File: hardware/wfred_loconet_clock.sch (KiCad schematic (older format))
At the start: 8 parts, among them U101 L6920D

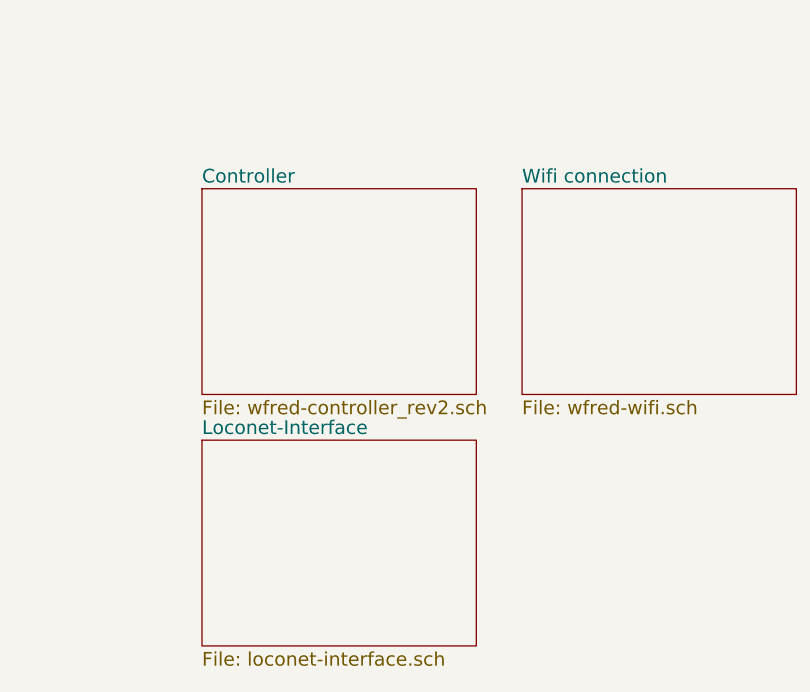
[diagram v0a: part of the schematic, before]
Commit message: Removed wiFred info from from clock project
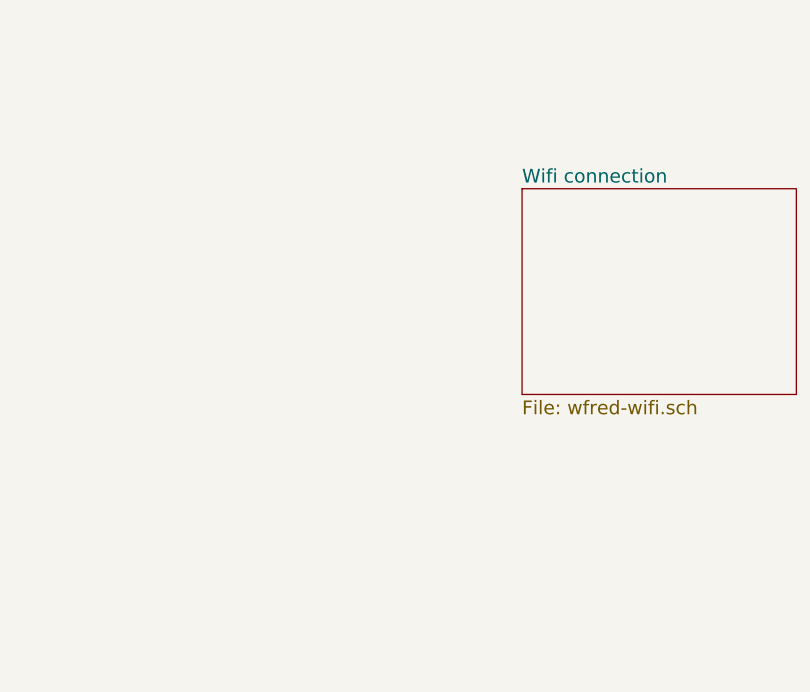
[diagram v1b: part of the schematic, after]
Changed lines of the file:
@@
 $Descr A4 11693 8268
 encoding utf-8
-Sheet 1 5
+Sheet 1 3
 Title "Wireless FREDI (and clock interface)"
 Date "2017-11-19"
@@
 	1    0    0    -1
 $EndComp
-$Sheet
-S 4700 4200 1200 900
-U 5920C945
-F0 "Controller" 60
-F1 "wfred-controller_rev2.sch" 60
-$EndSheet
-$Sheet
-S 4700 5300 1200 900
-U 5920DD06
-F0 "Loconet-Interface" 60
-F1 "loconet-interface.sch" 60
-$EndSheet
 $Comp
 L C C102

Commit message: Fix schematic after untangling from wiFred
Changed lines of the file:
@@
 $EndDescr
-Wire Wire Line
-	2450 2450 2450 2700
-Wire Wire Line
-	900  2600 2450 2600
 Wire Wire Line
 	2150 2400 2150 2700
@@
 Wire Wire Line
 	1500 2800 1850 2800
-Wire Wire Line
-	1850 2450 1850 3300
 Wire Wire Line
 	2150 3100 2150 3300
@@
 	1    0    0    -1
 $EndComp
-$Comp
-L PWR_FLAG #FLG011
-U 1 1 59214833
-P 2450 2450
-F 0 "#FLG011" H 2450 2545 30  0001 C CNN
-F 1 "PWR_FLAG" H 2450 2630 30  0000 C CNN
-F 2 "" H 2450 2450 60  0001 C CNN
-F 3 "" H 2450 2450 60  0001 C CNN
-	1    2450 2450
-	1    0    0    -1
-$EndComp
-Connection ~ 2450 2600
-$Comp
-L PWR_FLAG #FLG012
-U 1 1 59214BB2
-P 1850 2450
-F 0 "#FLG012" H 1850 2545 30  0001 C CNN
-F 1 "PWR_FLAG" H 1850 2630 30  0000 C CNN
-F 2 "" H 1850 2450 60  0001 C CNN
-F 3 "" H 1850 2450 60  0001 C CNN
-	1    1850 2450
-	1    0    0    -1
-$EndComp
-Connection ~ 1850 2800
 $Comp
 L L6920D U101
@@
 	0    1    1    0
 $EndComp
+Wire Wire Line
+	2450 2700 2450 2600
+Wire Wire Line
+	2450 2600 900  2600
+Wire Wire Line
+	1850 2800 1850 3300
 $EndSCHEMATC

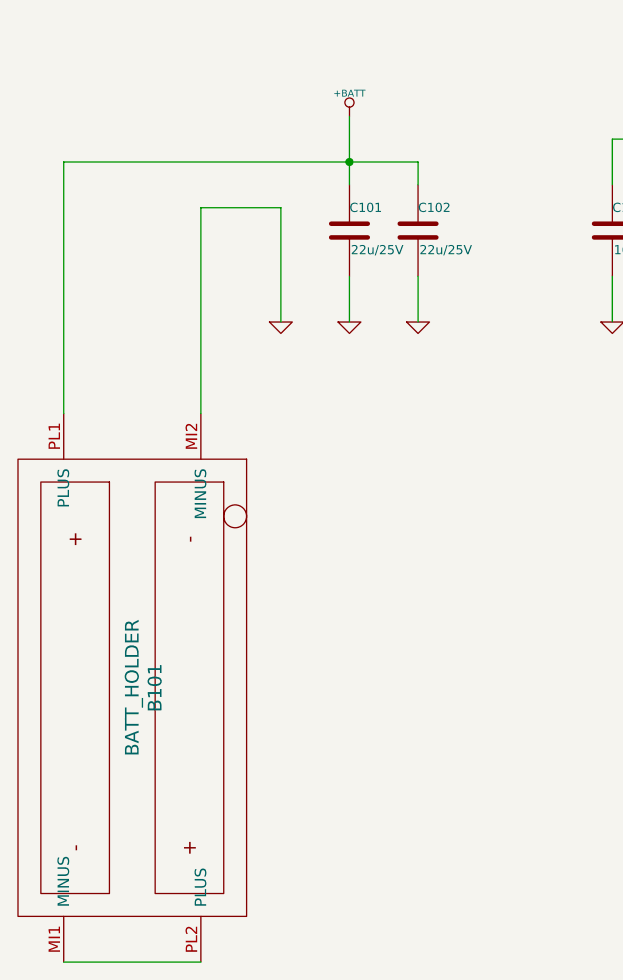
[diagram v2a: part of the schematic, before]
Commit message: Change clock schematic and PCB
- Remove slide switches, replace with single push button
- Add status LED
- Re-add battery measurement connection

- Change PCB form factor to fit NewAgeEnclosures Compact AA housing
- Re-layout PCB
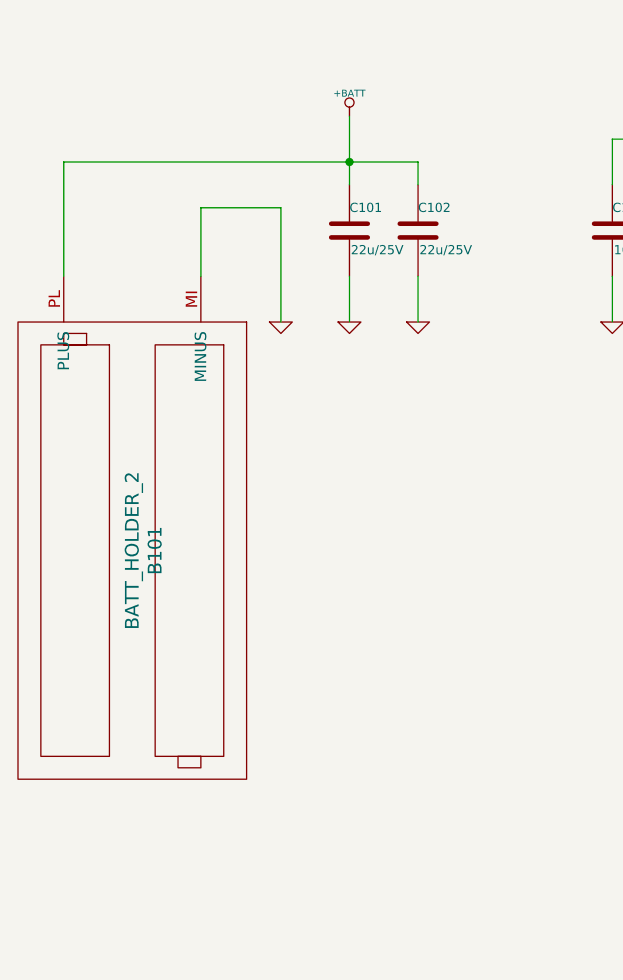
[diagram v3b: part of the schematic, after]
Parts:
- removed B101: BATT_HOLDER, myFootprints:KEYSTONE1013, symbol BATT_HOLDER
- added B101: BATT_HOLDER_2, myFootprints:NEW_AGE_COMPACT_AA_PCBEdges, symbol BATT_HOLDER_2
- L101: footprint myFootprints:L_2424_HandSoldering -> Inductors_SMD:L_Fastron_PISN_Handsoldering
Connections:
- net +BATT: now also B101.PL (PLUS)
- net GND: now also B101.MI (MINUS)
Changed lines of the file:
@@
 Connection ~ 2150 2600
-Wire Wire Line
-	1500 2800 1850 2800
 Wire Wire Line
 	2150 3100 2150 3300
@@
 F 0 "L101" V 4250 1400 40  0000 C CNN
 F 1 "22u" V 4400 1400 40  0000 C CNN
-F 2 "myFootprints:L_2424_HandSoldering" H 4300 1400 60  0001 C CNN
+F 2 "Inductors_SMD:L_Fastron_PISN_Handsoldering" H 4300 1400 60  0001 C CNN
 F 3 "" H 4300 1400 60  0000 C CNN
 F 4 "L-242418FPS 22µ" V 4300 1400 60  0001 C CNN "Reichelt"
@@
 $EndSheet
 Wire Wire Line
-	900  6100 1500 6100
-Wire Wire Line
-	900  3700 900  2600
-Wire Wire Line
-	1500 3700 1500 2800
-$Comp
-L BATT_HOLDER B101
-U 1 1 5A14A6C1
-P 1200 4900
-F 0 "B101" H 1200 5000 60  0000 C CNN
-F 1 "BATT_HOLDER" H 1200 4900 60  0000 C CNN
-F 2 "myFootprints:KEYSTONE1013" H 1200 4900 60  0001 C CNN
-F 3 "" H 1200 4900 60  0001 C CNN
-F 4 "KEYSTONE 1013" H 1200 4900 60  0001 C CNN "Reichelt"
-	1    1200 4900
+	2450 2600 2450 2700
+Wire Wire Line
+	1850 2800 1850 3300
+$Comp
+L BATT_HOLDER_2 B101
+U 1 1 5C82AFB3
+P 1200 4300
+F 0 "B101" H 1200 4400 60  0000 C CNN
+F 1 "BATT_HOLDER_2" H 1200 4300 60  0000 C CNN
+F 2 "myFootprints:NEW_AGE_COMPACT_AA_PCBEdges" H 1200 4300 60  0001 C CNN
+F 3 "" H 1200 4300 60  0001 C CNN
+	1    1200 4300
 	0    1    1    0
 $EndComp
 Wire Wire Line
-	2450 2700 2450 2600
-Wire Wire Line
-	2450 2600 900  2600
-Wire Wire Line
-	1850 2800 1850 3300
+	1500 3100 1500 2800
+Wire Wire Line
+	1500 2800 1850 2800
+Wire Wire Line
+	900  2600 2450 2600
+Wire Wire Line
+	900  2600 900  3100
 $EndSCHEMATC

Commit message: Opened schematic and pcb with kicad 5.1.5...
...to update library table
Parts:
- B101: symbol BATT_HOLDER_2 -> wfred_loconet_clock-rescue:BATT_HOLDER_2
- C101, C102, C103, C104, C105: symbol C -> wfred_loconet_clock-rescue:C
- L101: symbol INDUCTOR -> wfred_loconet_clock-rescue:INDUCTOR
- U101: symbol L6920D -> wfred_loconet_clock-rescue:L6920D
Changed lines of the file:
@@
-EESchema Schematic File Version 2
-LIBS:wfred_loconet_clock-rescue
-LIBS:power
-LIBS:device
-LIBS:transistors
-LIBS:conn
-LIBS:linear
-LIBS:regul
-LIBS:74xx
-LIBS:cmos4000
-LIBS:adc-dac
-LIBS:memory
-LIBS:xilinx
-LIBS:microcontrollers
-LIBS:dsp
-LIBS:microchip
-LIBS:analog_switches
-LIBS:motorola
-LIBS:texas
-LIBS:intel
-LIBS:audio
-LIBS:interface
-LIBS:digital-audio
-LIBS:philips
-LIBS:display
-LIBS:cypress
-LIBS:siliconi
-LIBS:opto
-LIBS:atmel
-LIBS:contrib
-LIBS:valves
-LIBS:my_devices
-LIBS:ESP8266
-LIBS:wfred_loconet_clock-cache
-EELAYER 25 0
+EESchema Schematic File Version 4
+EELAYER 30 0
 EELAYER END
 $Descr A4 11693 8268
@@
 $EndDescr
 Wire Wire Line
-	2150 2400 2150 2700
+	2150 2400 2150 2600
 Connection ~ 2150 2600
 Wire Wire Line
@@
 	3300 3100 3300 3300
 Wire Wire Line
-	5200 2000 5200 2800
-Wire Wire Line
-	5000 2200 6600 2200
+	5200 2000 5200 2200
+Wire Wire Line
+	5000 2200 5200 2200
 Wire Wire Line
 	5200 2800 5000 2800
@@
 Connection ~ 5500 2200
 $Comp
-L C C101
+L wfred_loconet_clock-rescue:C C101
 U 1 1 5920B38E
 P 2150 2900
@@
 $EndComp
 $Comp
-L GND #PWR01
+L wfred_loconet_clock-rescue:GND #PWR01
 U 1 1 5920B390
 P 2150 3300
@@
 $EndComp
 $Comp
-L GND #PWR02
+L wfred_loconet_clock-rescue:GND #PWR02
 U 1 1 5920B391
 P 1850 3300
@@
 $EndComp
 $Comp
-L GND #PWR03
+L wfred_loconet_clock-rescue:GND #PWR03
 U 1 1 5920B392
 P 2450 3300
@@
 $EndComp
 $Comp
-L +BATT #PWR04
+L wfred_loconet_clock-rescue:+BATT #PWR04
 U 1 1 5920B394
 P 2150 2400
@@
 $EndComp
 $Comp
-L INDUCTOR L101
+L wfred_loconet_clock-rescue:INDUCTOR L101
 U 1 1 5920B395
 P 4300 1400
@@
 $EndComp
 $Comp
-L +BATT #PWR05
+L wfred_loconet_clock-rescue:+BATT #PWR05
 U 1 1 5920B396
 P 4300 900
@@
 NoConn ~ 3600 2200
 $Comp
-L C C103
+L wfred_loconet_clock-rescue:C C103
 U 1 1 5920B397
 P 3300 2900
@@
 $EndComp
 $Comp
-L GND #PWR06
+L wfred_loconet_clock-rescue:GND #PWR06
 U 1 1 5920B398
 P 3300 3300
@@
 $EndComp
 $Comp
-L GND #PWR07
+L wfred_loconet_clock-rescue:GND #PWR07
 U 1 1 5920B399
 P 3500 3300
@@
 NoConn ~ 5000 2500
 $Comp
-L VCC #PWR08
+L wfred_loconet_clock-rescue:VCC #PWR08
 U 1 1 5920B39A
 P 5200 2000
@@
 $EndComp
 $Comp
-L GND #PWR09
+L wfred_loconet_clock-rescue:GND #PWR09
 U 1 1 5920B39D
 P 6300 3300
@@
 $EndComp
 $Comp
-L GND #PWR010
+L wfred_loconet_clock-rescue:GND #PWR010
 U 1 1 5920B39E
 P 6600 3300
@@
 $EndComp
 $Comp
-L C C102
+L wfred_loconet_clock-rescue:C C102
 U 1 1 59210DD0
 P 2450 2900
@@
 $EndComp
 $Comp
-L C C104
+L wfred_loconet_clock-rescue:C C104
 U 1 1 59210E13
 P 6300 2600
@@
 $EndComp
 $Comp
-L C C105
+L wfred_loconet_clock-rescue:C C105
 U 1 1 59210E8B
 P 6600 2600
@@
 $EndComp
 $Comp
-L L6920D U101
+L wfred_loconet_clock-rescue:L6920D U101
 U 1 1 5920B393
 P 4300 2500
@@
 	1850 2800 1850 3300
 $Comp
-L BATT_HOLDER_2 B101
+L wfred_loconet_clock-rescue:BATT_HOLDER_2 B101
 U 1 1 5C82AFB3
 P 1200 4300
@@
 	1500 2800 1850 2800
 Wire Wire Line
-	900  2600 2450 2600
+	900  2600 2150 2600
 Wire Wire Line
 	900  2600 900  3100
+Wire Wire Line
+	2150 2600 2150 2700
+Wire Wire Line
+	2150 2600 2450 2600
+Wire Wire Line
+	5200 2200 5200 2800
+Wire Wire Line
+	5200 2200 5500 2200
+Wire Wire Line
+	6300 2200 6600 2200
+Wire Wire Line
+	5500 2200 6300 2200
 $EndSCHEMATC
